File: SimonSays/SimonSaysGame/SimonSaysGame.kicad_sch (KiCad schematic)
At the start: 22 parts, among them SW1 SW_Push, SW2 SW_Push, SW3 SW_Push, SW4 SW_Push, X1 Crystal

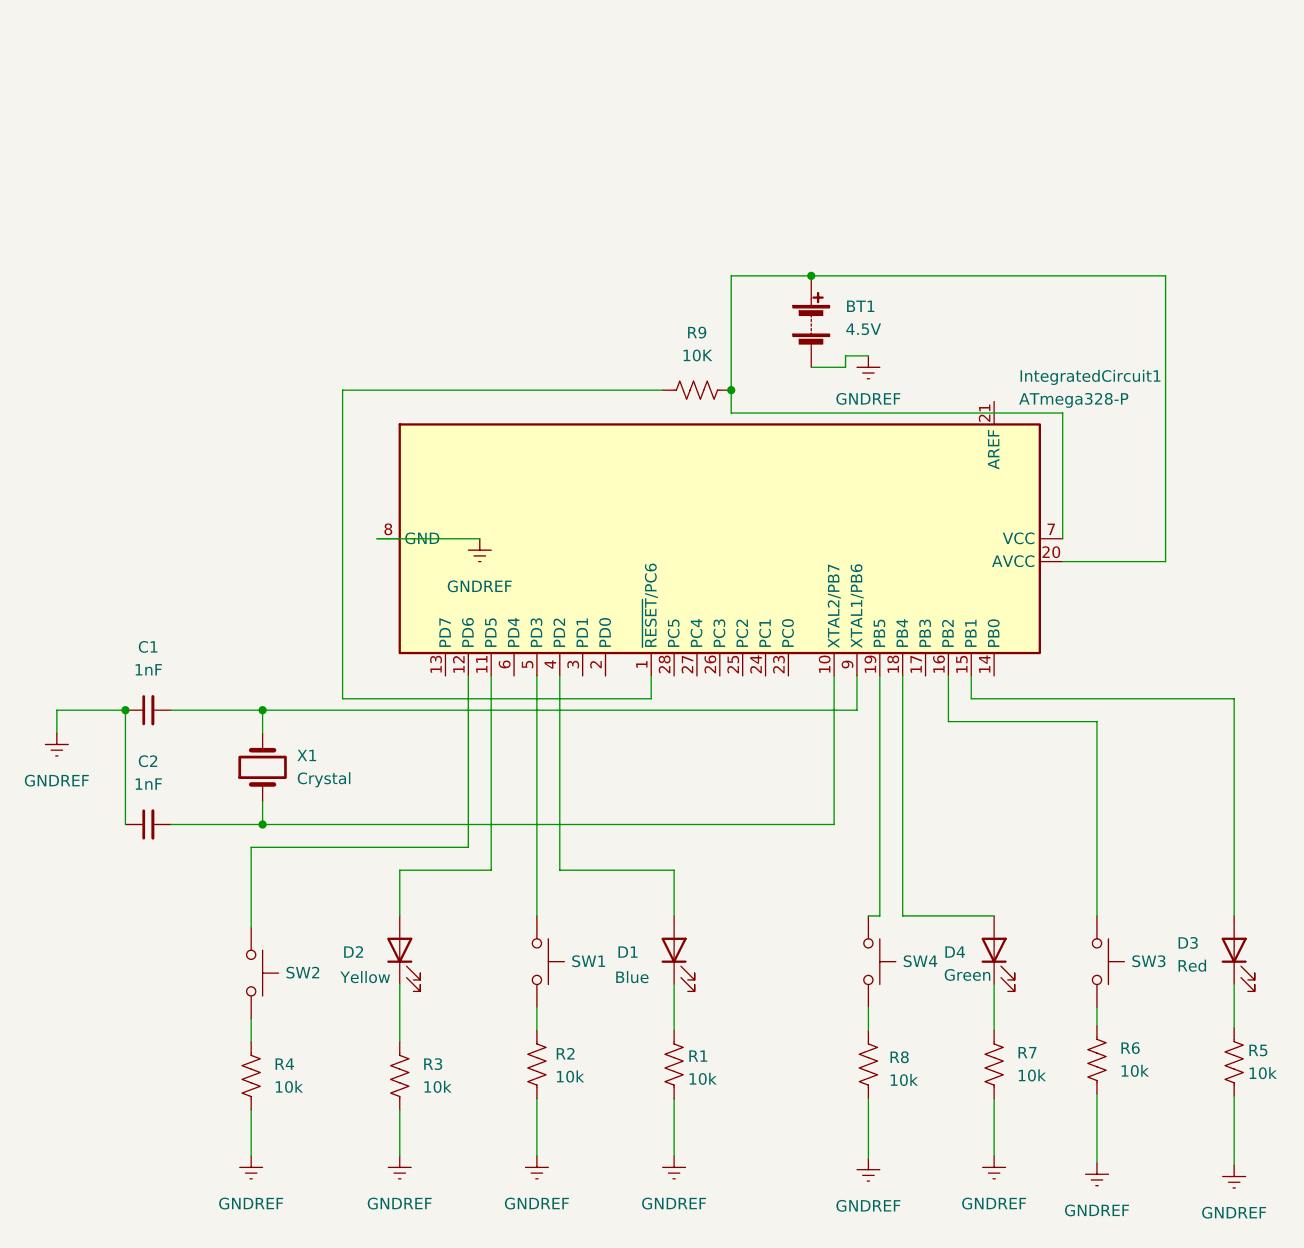
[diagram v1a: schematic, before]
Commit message: changed switches to tactile
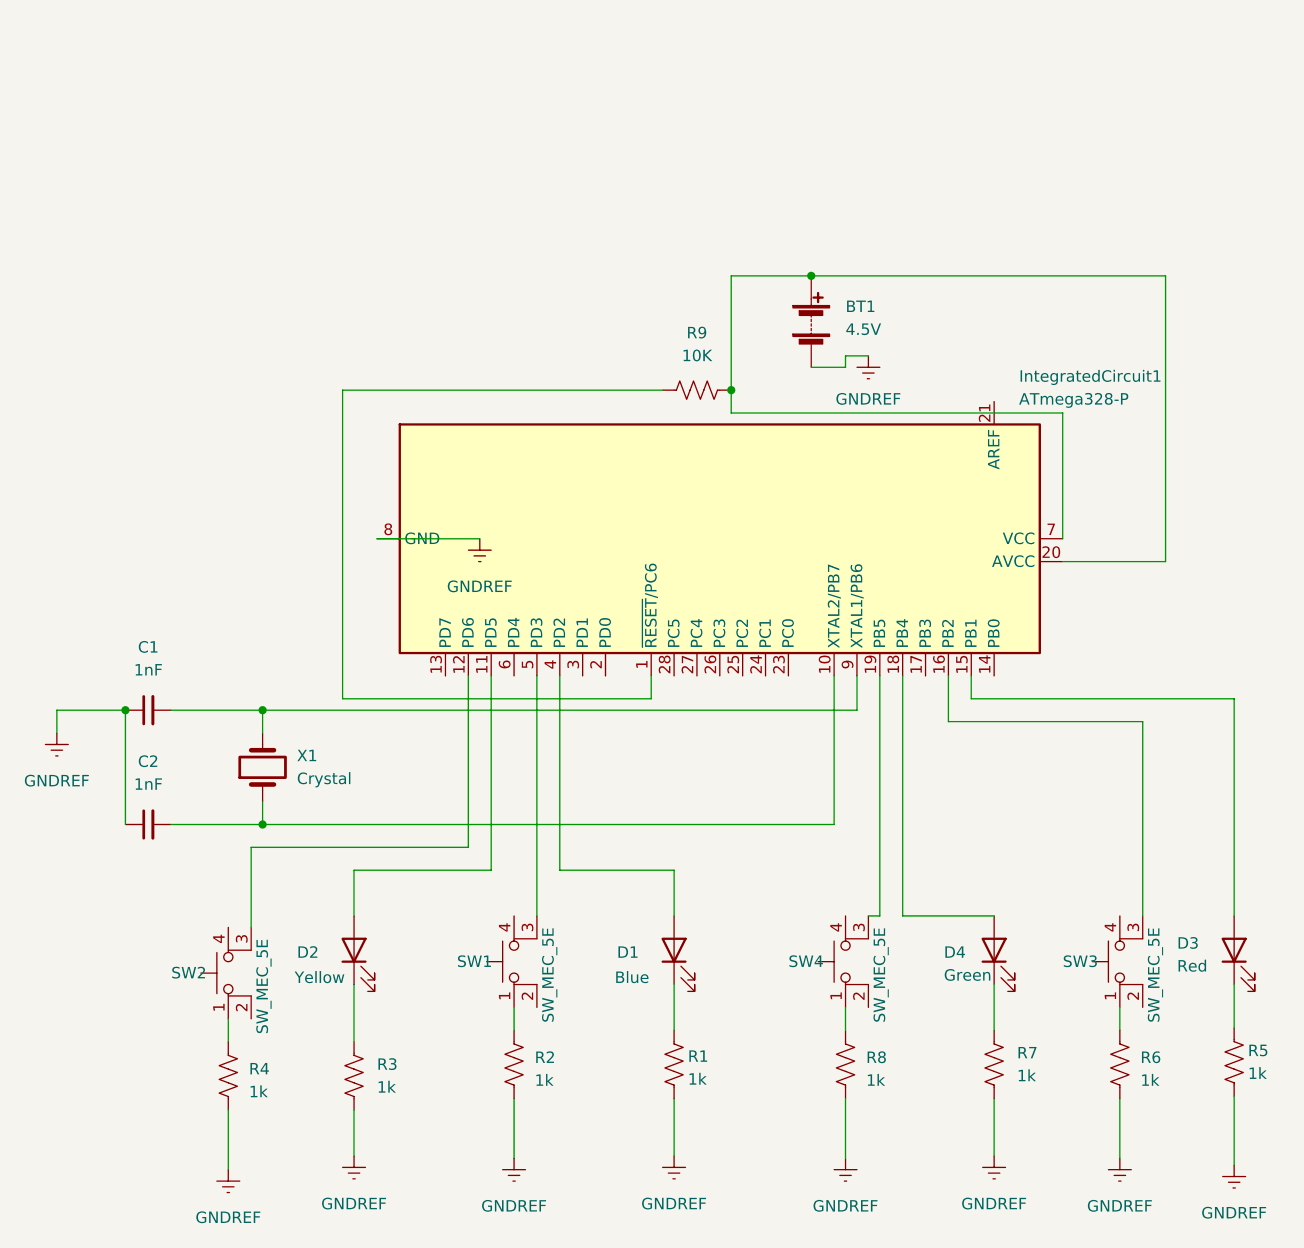
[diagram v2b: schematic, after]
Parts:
- removed SW1, SW2, SW3, SW4: SW_Push, Button_Switch_THT:SW_TH_Tactile_Omron_B3F-10xx, symbol Switch:SW_Push
- added SW1, SW2, SW3, SW4: SW_MEC_5E, symbol Switch:SW_MEC_5E
- R1, R2, R3, R4, R5, R6, R7, R8: value 10k -> 1k
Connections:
- net at R2.1: now also SW1.1
- net at IntegratedCircuit1.16 (PB2): now also SW3.3 (K)
- net at R6.1: now also SW3.1
- net at R4.1: now also SW2.1
- net at IntegratedCircuit1.5 (PD3): now also SW1.3 (K)
- net at R8.1: now also SW4.1
- net at IntegratedCircuit1.12 (PD6): now also SW2.3 (K)
- net at IntegratedCircuit1.19 (PB5): now also SW4.3 (K)
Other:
- moved on the sheet: D2, R3, R8

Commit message: undo switch change
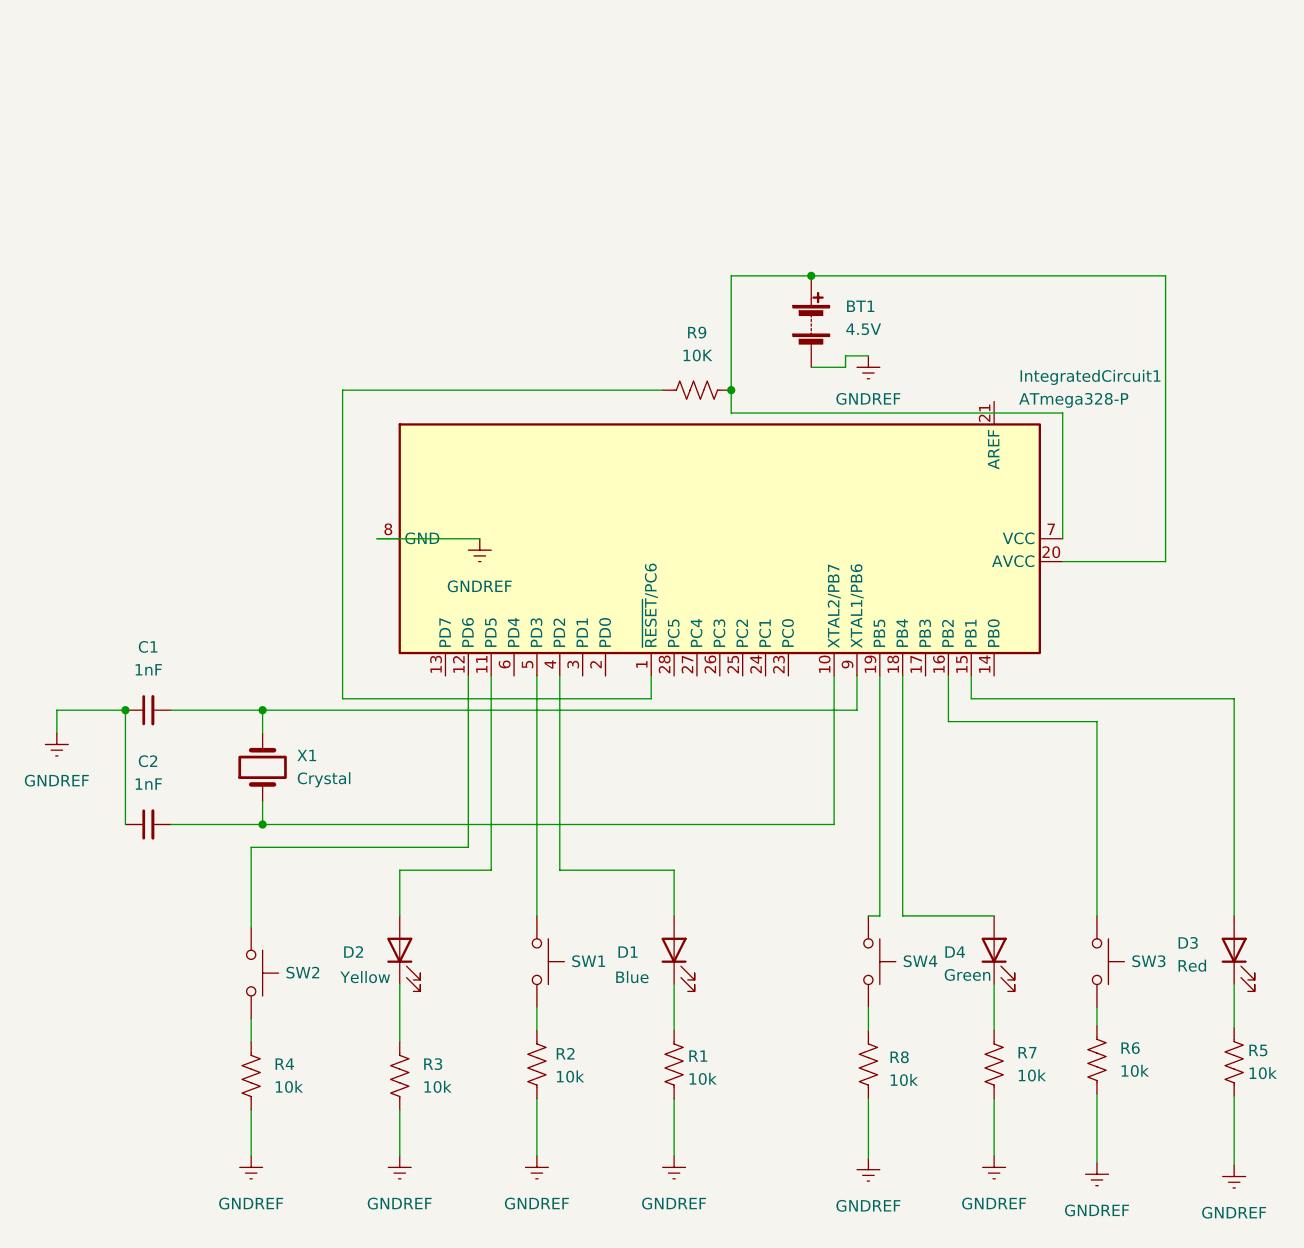
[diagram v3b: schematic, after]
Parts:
- removed SW1, SW2, SW3, SW4: SW_MEC_5E, symbol Switch:SW_MEC_5E
- added SW1, SW2, SW3, SW4: SW_Push, Button_Switch_THT:SW_TH_Tactile_Omron_B3F-10xx, symbol Switch:SW_Push
- R1, R2, R3, R4, R5, R6, R7, R8: value 1k -> 10k
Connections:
- net at R4.1: now also SW2.2
- net at R2.1: now also SW1.2
- net at R6.1: now also SW3.2
- net at R8.1: now also SW4.2
- net at IntegratedCircuit1.19 (PB5): now also SW4.1
- net at IntegratedCircuit1.16 (PB2): now also SW3.1
- net at IntegratedCircuit1.12 (PD6): now also SW2.1
- net at IntegratedCircuit1.5 (PD3): now also SW1.1
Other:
- moved on the sheet: D2, R3, R8

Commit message: added
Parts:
- removed BT1: 4.5V, Battery:BatteryHolder_Keystone_2479_3xAAA, symbol Device:Battery
- added BT1: Battery_Cell, Battery:BatteryHolder_Keystone_106_1x20mm, symbol Device:Battery_Cell
- added D1: DIODE, Diode_THT:D_DO-15_P15.24mm_Horizontal, symbol pspice:DIODE
- added F1: Fuse, Fuse:Fuseholder_Cylinder-5x20mm_EATON_H15-V-1_Vertical_Closed, symbol Device:Fuse
- added SW1: SW_DIP_x01, symbol Switch:SW_DIP_x01
- R1, R3, R5, R7: value 10k -> 1k
- SW1, SW2, SW3, SW4: footprint Button_Switch_THT:SW_TH_Tactile_Omron_B3F-10xx -> Button_Switch_THT:SW_PUSH_6mm_H4.3mm
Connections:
- net GNDREF: now also BT1.2 (-)
- net at IntegratedCircuit1.20 (AVCC), IntegratedCircuit1.7 (VCC), R9.2: now also D1.2 (A)
- new net: BT1.1 (+), SW1.1
- new net: D1.1 (K), F1.1
- new net: F1.2, SW1.2
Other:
- moved on the sheet: R8, SW4
